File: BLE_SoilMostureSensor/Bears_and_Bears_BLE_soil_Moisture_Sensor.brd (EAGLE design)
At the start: 33.6 x 78.4 mm, 47 parts, among them Q1 2N3904, U2 EFR32BG13

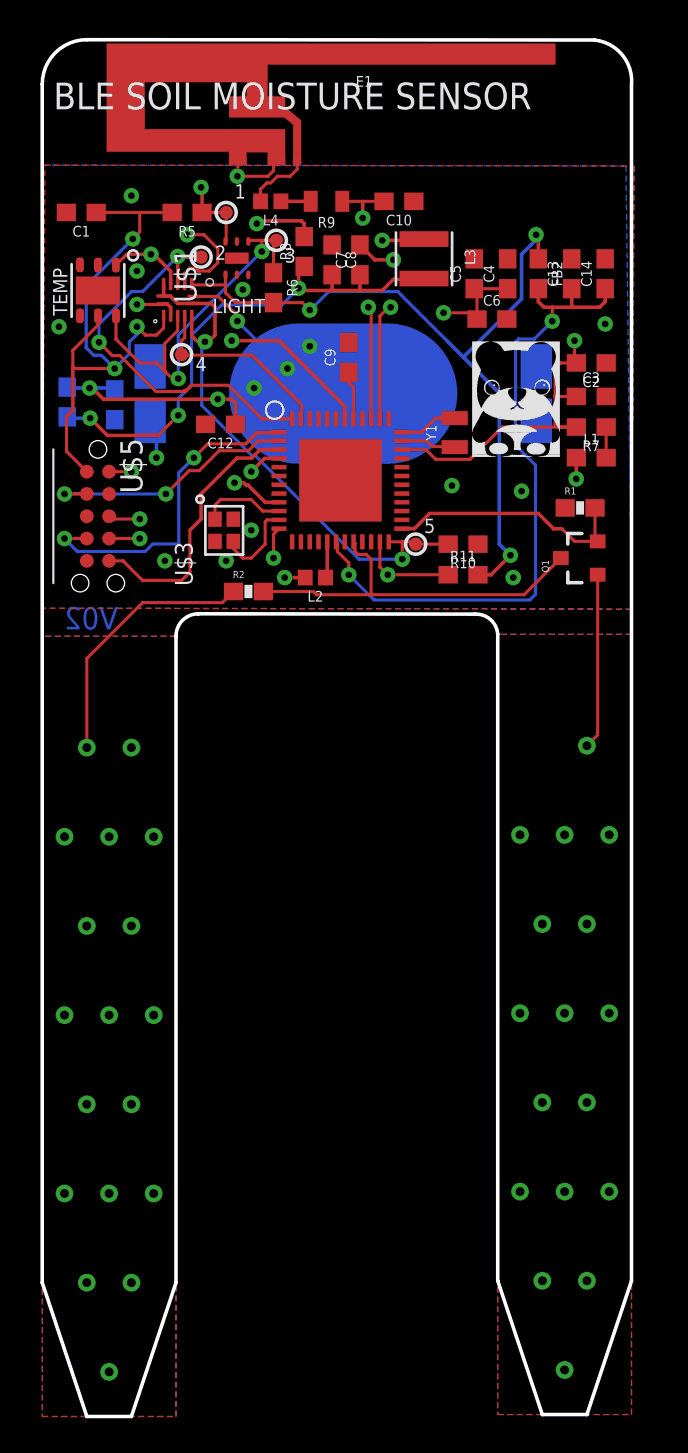
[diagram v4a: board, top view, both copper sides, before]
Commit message: 1. MDE BOARD SMALLER, RE DID LAYOUT, DELETED SILK. TO DO: REPLACE SILK, FINISH ROUTING, POLYGON PROCESSING, IN DEPTH DESIGN REVIEW, REVIEW nrf ANTENNA REQUIREMENT AND LAYOUT SUGGESTIONS
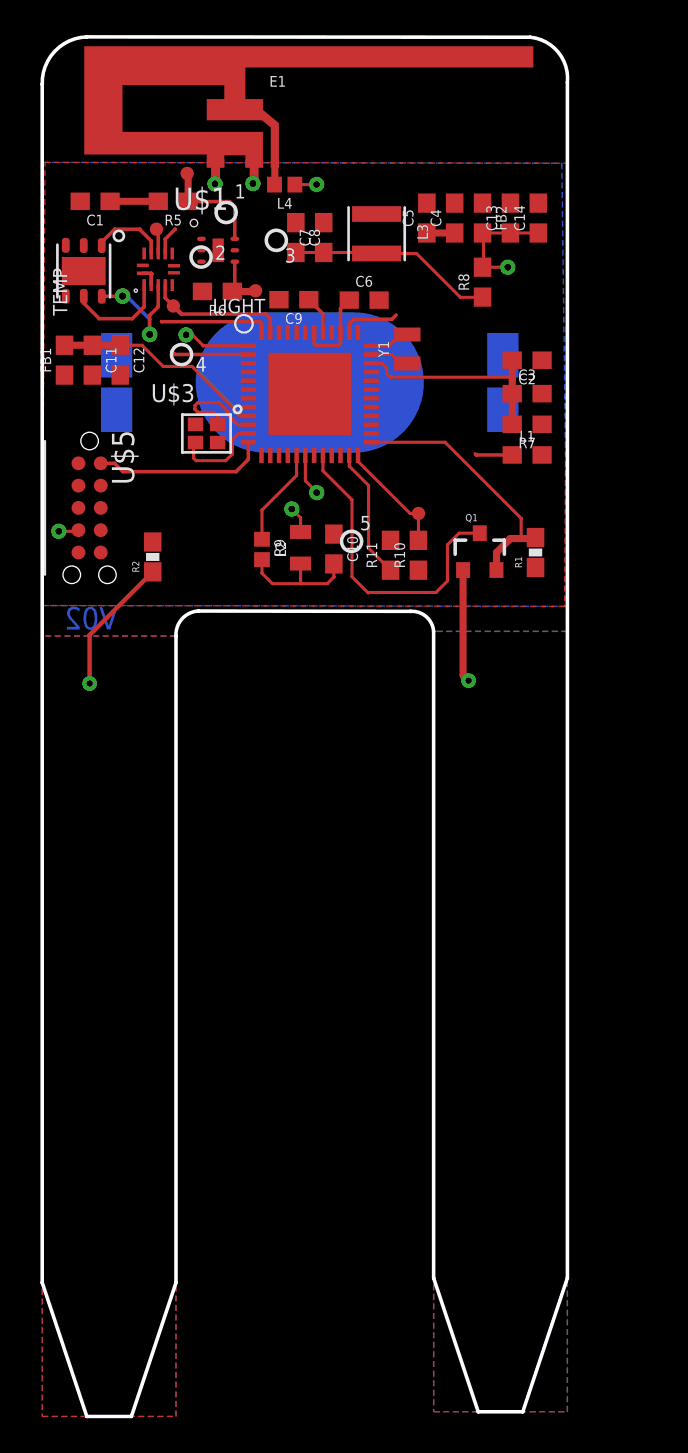
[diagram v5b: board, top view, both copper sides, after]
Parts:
- removed U$4: IMAGES#JPG, images#jpg(2):IMAGES#JPG
- moved C10 20.1 mm to (55.3, 49.7), turned to 270 degrees
- moved R9 19.8 mm to (53.5, 49.8), turned to 90 degrees
- moved R8 10.3 mm to (63.8, 64.9)
- moved C6 7.36 mm to (57.1, 63.9)
- moved C12 6.78 mm to (43.2, 60.5), turned to 270 degrees
- moved U$3 6.76 mm to (47.5, 56.8), turned to 0 degrees
- moved R2 5.80 mm to (45.0, 49.3), turned to 90 degrees
- moved Q1 5.72 mm to (63.7, 49.5), turned to 0 degrees
- moved Y1 5.47 mm to (59.5, 61.1)
- moved U2 5.22 mm to (54.0, 57.3)
- moved C14 4.96 mm to (67.0, 68.6)
- moved C13 4.72 mm to (65.4, 68.6)
- moved C9 4.54 mm to (53.1, 63.9), turned to 180 degrees
- moved FB2 4.49 mm to (63.8, 68.6)
- moved C4 4.38 mm to (62.2, 68.6)
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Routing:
- net VDD: track 90.5 -> 8.45 mm, vias 6 -> 0
- net N$23: track 1.70 -> 48.3 mm, vias 0 -> 2
- net V_BATT: track 57.3 -> 11.4 mm, vias 7 -> 0
- net PAVDD: track 66.8 -> 26.3 mm, vias 3 -> 2
- net SENSOR_ENABLE: track 31.7 -> 6.54 mm, vias 2 -> 0
- net N$3: track 26.8 -> 7.19 mm, vias 2 -> 0
- net VDCDC: track 30.0 -> 11.7 mm, vias 3 -> 0
- net SDA: track 23.3 -> 7.67 mm, vias 2 -> 0
- net TDO: track 15.5 -> 0.00 mm
- net GND_DETECT: track 22.2 -> 7.51 mm, vias 2 -> 0
- net GND: track 17.0 -> 2.34 mm, vias 17 -> 2
- net SCL_IN: track 23.0 -> 10.3 mm
- net TDI: track 12.1 -> 0.00 mm, vias 2 -> 0
- net TMS: track 14.9 -> 4.46 mm, vias 2 -> 0
- net VREGSW: track 13.4 -> 3.38 mm, vias 2 -> 0
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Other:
- board size 33.6 x 78.4 mm -> 29.9 x 78.6 mm
- board text removed: "BLE SOIL MOISTURE SENSOR"

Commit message: Delete bad polygons
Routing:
- removed copper zone on layer 16, net GND
- removed copper zone on layer 2, net GND
- removed copper zone on layer 15, net V_BATT
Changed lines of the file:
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@@
 <?xml version="1.0" encoding="utf-8"?>
 <!DOCTYPE eagle SYSTEM "eagle.dtd">
-<eagle version="9.1.0">
+<eagle version="9.2.2">
 <drawing>
 <settings>
@@
 <contactref element="U$3" pad="GND2"/>
 <contactref element="U2" pad="16"/>
-<polygon width="0.2032" layer="1">
-<vertex x="38.8947125" y="71.749471875"/>
-<vertex x="68.64985" y="71.704440625"/>
-<vertex x="68.4911" y="46.463190625"/>
-<vertex x="38.7359625" y="46.508221875"/>
-<vertex x="38.735" y="46.355"/>
-</polygon>
-<polygon width="0.2032" layer="16">
-<vertex x="38.735" y="71.749421875"/>
-<vertex x="68.33235" y="71.7042"/>
-<vertex x="68.64985" y="46.46295"/>
-<vertex x="38.735" y="46.508225"/>
-<vertex x="38.735" y="46.355"/>
-</polygon>
 <contactref element="U2" pad="GND"/>
 <contactref element="U2" pad="37"/>
 <contactref element="U2" pad="14"/>
 <contactref element="U2" pad="15"/>
-<polygon width="0.2032" layer="2" rank="2">
-<vertex x="38.894746875" y="71.755"/>
-<vertex x="68.8975" y="71.755"/>
-<vertex x="68.73875" y="46.51375"/>
-<vertex x="38.735996875" y="46.51375"/>
-<vertex x="38.735" y="46.355"/>
-</polygon>
 <contactref element="E1" pad="GND2"/>
 <contactref element="U$5" pad="3"/>
@@
 <wire x1="50.80745" y1="70.61945" x2="50.80745" y2="71.68655" width="0.508" layer="1"/>
 <wire x1="50.7365" y1="70.5485" x2="50.80745" y2="70.61945" width="0.508" layer="1"/>
-<wire x1="65.405" y1="69.43" x2="66.9925" y2="69.43" width="0" layer="19" extent="1-1"/>
-<wire x1="62.23" y1="69.43" x2="65.405" y2="69.43" width="0" layer="19" extent="1-1"/>
-<wire x1="60.6425" y1="69.43" x2="62.23" y2="69.43" width="0" layer="19" extent="1-1"/>
-<wire x1="54.76875" y1="68.31875" x2="60.6425" y2="69.43" width="0" layer="19" extent="1-1"/>
-<wire x1="53.18125" y1="68.31875" x2="54.76875" y2="68.31875" width="0" layer="19" extent="1-1"/>
-<wire x1="50.80745" y1="70.61945" x2="53.18125" y2="68.31875" width="0" layer="19" extent="1-1"/>
-<wire x1="48.60745" y1="70.5546375" x2="50.7365" y2="70.5485" width="0" layer="19" extent="1-1"/>
-<wire x1="48.754375" y1="66.745125" x2="48.5775" y2="70.5246875" width="0" layer="19" extent="1-1"/>
-<wire x1="47.804375" y1="66.745125" x2="48.754375" y2="66.745125" width="0" layer="19" extent="1-1"/>
-<wire x1="47.804375" y1="66.095125" x2="47.804375" y2="66.745125" width="0" layer="19" extent="1-1"/>
-<wire x1="46.24125" y1="65.86125" x2="47.804375" y2="66.095125" width="0" layer="19" extent="1-1"/>
-<wire x1="52.220125" y1="63.928625" x2="48.754375" y2="66.745125" width="0" layer="19" extent="1-1"/>
-<wire x1="56.725" y1="62.05875" x2="52.220125" y2="63.928625" width="0" layer="19" extent="1-1"/>
+<polygon width="0.1524" layer="1">
+<vertex x="38.6318125" y="71.4375"/>
+<vertex x="38.6318125" y="46.720125"/>
+<vertex x="38.719125" y="46.6328125"/>
+<vertex x="68.54825" y="46.6328125"/>
+<vertex x="68.6355625" y="46.720125"/>
+<vertex x="68.6355625" y="71.5248125"/>
+<vertex x="68.54825" y="71.5248125"/>
+</polygon>
+<wire x1="53.975" y1="58.55875" x2="53.975" y2="59.21375" width="0" layer="19" extent="1-16"/>
 <wire x1="57.9222125" y1="63.9064" x2="56.725" y2="62.05875" width="0" layer="19" extent="1-1"/>
-<wire x1="53.975" y1="59.21375" x2="56.725" y2="62.05875" width="0" layer="19" extent="1-16"/>
-<wire x1="53.975" y1="58.55875" x2="53.975" y2="59.21375" width="0" layer="19" extent="1-16"/>
-<wire x1="52.725" y1="55.05875" x2="53.975" y2="58.55875" width="0" layer="19" extent="1-1"/>
-<wire x1="52.225" y1="55.05875" x2="52.725" y2="55.05875" width="0" layer="19" extent="1-1"/>
-<wire x1="51.725" y1="55.05875" x2="52.225" y2="55.05875" width="0" layer="19" extent="1-1"/>
-<wire x1="48.72625" y1="55.7925" x2="51.725" y2="55.05875" width="0" layer="19" extent="1-1"/>
-<wire x1="47.46625" y1="56.8325" x2="48.72625" y2="55.7925" width="0" layer="19" extent="1-1"/>
+<wire x1="48.72625" y1="55.7925" x2="47.46625" y2="56.8325" width="0" layer="19" extent="1-1"/>
 <wire x1="55.3481875" y1="50.5784375" x2="52.725" y2="55.05875" width="0" layer="19" extent="1-1"/>
-<wire x1="43.18" y1="59.63375" x2="47.46625" y2="56.8325" width="0" layer="19" extent="1-1"/>
-<wire x1="41.5925" y1="59.63375" x2="43.18" y2="59.63375" width="0" layer="19" extent="1-1"/>
-<wire x1="60.16625" y1="48.52125" x2="55.3481875" y2="50.5784375" width="0" layer="19" extent="1-1"/>
-<wire x1="41.100375" y1="65.56375" x2="46.24125" y2="65.86125" width="0" layer="19" extent="1-1"/>
-<wire x1="41.100375" y1="67.01375" x2="41.100375" y2="65.56375" width="0" layer="19" extent="1-1"/>
-<wire x1="40.90125" y1="69.5325" x2="41.100375" y2="67.01375" width="0" layer="19" extent="1-1"/>
-<wire x1="66.83375" y1="48.68" x2="60.16625" y2="48.52125" width="0" layer="19" extent="1-1"/>
-<wire x1="40.79875" y1="52.07" x2="41.5925" y2="59.63375" width="0" layer="19" extent="1-1"/>
-<wire x1="40.79875" y1="49.53" x2="40.79875" y2="52.07" width="0" layer="19" extent="1-1"/>
-<wire x1="67.2075" y1="60.48375" x2="66.9925" y2="69.43" width="0" layer="19" extent="1-1"/>
-<wire x1="67.2075" y1="58.57875" x2="67.2075" y2="60.48375" width="0" layer="19" extent="1-1"/>
 </signal>
 <signal name="PROBE1">
@@
 <wire x1="46.14125" y1="66.56125" x2="47.804375" y2="67.395125" width="0" layer="19" extent="1-1"/>
 <wire x1="44.54125" y1="64.76125" x2="46.14125" y2="66.56125" width="0" layer="19" extent="1-1"/>
-<wire x1="47.8624375" y1="64.3969375" x2="47.804375" y2="67.395125" width="0" layer="19" extent="1-1"/>
+<wire x1="47.8624375" y1="64.3969375" x2="46.14125" y2="66.56125" width="0" layer="19" extent="1-1"/>
 <wire x1="45.34625" y1="69.5325" x2="46.14125" y2="66.56125" width="0" layer="19" extent="1-1"/>
 <wire x1="40.79875" y1="54.61" x2="41.9814375" y2="62.849125" width="0" layer="19" extent="1-1"/>
@@
 <contactref element="C6" pad="1"/>
 <contactref element="U2" pad="42"/>
-<polygon width="0.2032" layer="15" rank="2">
-<vertex x="38.73300625" y="71.755"/>
-<vertex x="68.58" y="71.755"/>
-<vertex x="68.73875" y="46.51375"/>
-<vertex x="38.89175625" y="46.51375"/>
-<vertex x="38.892753125" y="46.355"/>
-</polygon>
 <wire x1="62.23" y1="67.73" x2="60.6425" y2="67.73" width="0.4064" layer="1"/>
 <wire x1="44.46625" y1="65.43625" x2="44.9505625" y2="65.43625" width="0.2032" layer="1"/>

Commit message: routing completed and ready for review
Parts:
- added U$4: (no value), Capture#PNG (3):CAPTURE#PNG
- added U$6: (no value), buzzard_labels (7):INTERNET_OF_PLANTS0
- moved R6 4.19 mm to (51.5, 67.5), turned to 90 degrees
- moved TP2 3.97 mm to (50.2, 63.5)
- moved R2 3.58 mm to (48.5, 48.5)
- moved U$3 1.75 mm to (45.7, 56.7)
- moved U$1 1.64 mm to (48.1, 64.2)
- moved TP1 1.02 mm to (51.5, 65.2)
- moved TP4 0.05 mm to (45.3, 68.0)
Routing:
- net VDD: track 8.45 -> 97.3 mm, vias 0 -> 7
- net SENSOR_ENABLE: track 6.54 -> 42.9 mm, vias 0 -> 3
- net PROBE2: track 7.85 -> 42.9 mm, vias 1 -> 109
- net VDCDC: track 11.7 -> 41.6 mm, vias 0 -> 2
- net TDO: track 0.00 -> 22.9 mm, vias 0 -> 2
- net GND_DETECT: track 7.51 -> 25.8 mm, vias 0 -> 2
- net TDI: track 0.00 -> 16.7 mm, vias 0 -> 2
- net SDA: track 7.67 -> 21.8 mm, vias 0 -> 2
- net TMS: track 4.46 -> 18.0 mm, vias 0 -> 2
- net SDA_IN: track 10.6 -> 22.2 mm
- net VREGSW: track 3.38 -> 14.5 mm, vias 0 -> 2
- net SOIL_MOIST_PWR: track 18.0 -> 27.6 mm
- net V_BATT: track 11.4 -> 19.3 mm, vias 0 -> 6
- net TCK: track 21.1 -> 28.4 mm
- net SCL_IN: track 10.3 -> 17.1 mm, vias 2 -> 3
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- added copper zone on layer 16, net GND
- added copper zone on layer 2, net GND
- added copper zone on layer 15, net V_BATT
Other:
- board text removed: "1"
- board text removed: "2"
- board text removed: "4"
- board text removed: "5"
